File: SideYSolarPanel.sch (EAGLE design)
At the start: 35 parts

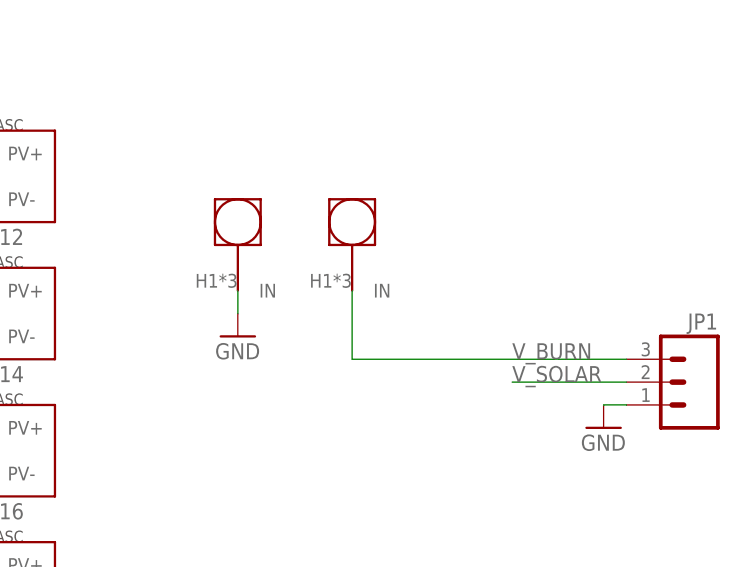
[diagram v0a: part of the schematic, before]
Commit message: Swapped X and Y solar panels per NanoRacks ICD
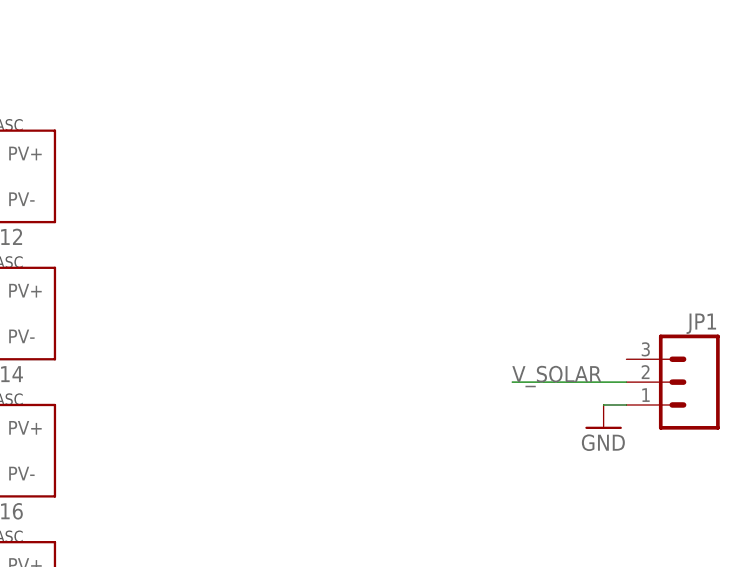
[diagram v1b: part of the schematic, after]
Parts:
- removed U$1, U$2: BURNER, Burner:BURNER
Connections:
- removed net V_BURN: JP1.3, U$1.IN
- net GND: no longer U$2.IN
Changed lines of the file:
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@@
 <part name="GND2" library="SparkFun" deviceset="GND" device=""/>
 <part name="JP1" library="SparkFun-Connectors" deviceset="M03" device="POLAR_LOCK"/>
-<part name="U$1" library="Burner" deviceset="BURNER" device=""/>
-<part name="U$2" library="Burner" deviceset="BURNER" device=""/>
-<part name="GND3" library="SparkFun" deviceset="GND" device=""/>
 </parts>
 <sheets>
@@
 <instance part="GND2" gate="1" x="172.72" y="60.96"/>
 <instance part="JP1" gate="G$1" x="182.88" y="66.04" rot="MR0"/>
-<instance part="U$1" gate="G$1" x="144.78" y="81.28"/>
-<instance part="U$2" gate="G$1" x="132.08" y="81.28"/>
-<instance part="GND3" gate="1" x="132.08" y="71.12"/>
 </instances>
 <busses>
@@
 <wire x1="172.72" y1="63.5" x2="175.26" y2="63.5" width="0.1524" layer="91"/>
 </segment>
-<segment>
-<pinref part="GND3" gate="1" pin="GND"/>
-<pinref part="U$2" gate="G$1" pin="IN"/>
-<wire x1="132.08" y1="73.66" x2="132.08" y2="76.2" width="0.1524" layer="91"/>
-</segment>
 </net>
 <net name="N$36" class="0">
@@
 </segment>
 </net>
-<net name="V_BURN" class="0">
-<segment>
-<pinref part="JP1" gate="G$1" pin="3"/>
-<label x="162.56" y="68.58" size="1.778" layer="95"/>
-<pinref part="U$1" gate="G$1" pin="IN"/>
-<wire x1="175.26" y1="68.58" x2="144.78" y2="68.58" width="0.1524" layer="91"/>
-<wire x1="144.78" y1="68.58" x2="144.78" y2="76.2" width="0.1524" layer="91"/>
-</segment>
-</net>

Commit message: Cleanup
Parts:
- added FRAME1: FRAME-LETTER, SparkFun-Aesthetics:FRAME-LETTER
- added U$1: KICKSAT_LOGO, KickSat-Logo:KICKSAT_LOGO
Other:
- note added: "Zac Manchester"
- moved on the sheet: D1, D10, D11, D12, D2, D3, D4, D5, D6, D7, D8, D9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

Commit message: Fixed solar cell footprints
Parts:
- D1, D10, D11, D12, D2, D3, D4, D5, D6, D7, D8, D9: device phonesat:SB_DIODE -> Solar:SB_DIODE
- S1, S10, S11, S12, S13, S14, S15, S16, S17, S18, S19, S2, S20, S3, S4, S5, S6, S7, S8, S9: device phonesat:SOLAR_CELL -> Solar:SOLAR_CELL
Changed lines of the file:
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@@
 </classes>
 <parts>
-<part name="S3" library="phonesat" deviceset="SOLAR_CELL" device=""/>
-<part name="D2" library="phonesat" deviceset="SB_DIODE" device=""/>
-<part name="S18" library="phonesat" deviceset="SOLAR_CELL" device=""/>
-<part name="S17" library="phonesat" deviceset="SOLAR_CELL" device=""/>
-<part name="S2" library="phonesat" deviceset="SOLAR_CELL" device=""/>
-<part name="S19" library="phonesat" deviceset="SOLAR_CELL" device=""/>
-<part name="S20" library="phonesat" deviceset="SOLAR_CELL" device=""/>
-<part name="S1" library="phonesat" deviceset="SOLAR_CELL" device=""/>
-<part name="S15" library="phonesat" deviceset="SOLAR_CELL" device=""/>
-<part name="S4" library="phonesat" deviceset="SOLAR_CELL" device=""/>
-<part name="S8" library="phonesat" deviceset="SOLAR_CELL" device=""/>
-<part name="S7" library="phonesat" deviceset="SOLAR_CELL" device=""/>
-<part name="S9" library="phonesat" deviceset="SOLAR_CELL" device=""/>
-<part name="S10" library="phonesat" deviceset="SOLAR_CELL" device=""/>
-<part name="S5" library="phonesat" deviceset="SOLAR_CELL" device=""/>
-<part name="S6" library="phonesat" deviceset="SOLAR_CELL" device=""/>
-<part name="D1" library="phonesat" deviceset="SB_DIODE" device=""/>
-<part name="D3" library="phonesat" deviceset="SB_DIODE" device=""/>
-<part name="D4" library="phonesat" deviceset="SB_DIODE" device=""/>
-<part name="D5" library="phonesat" deviceset="SB_DIODE" device=""/>
-<part name="D6" library="phonesat" deviceset="SB_DIODE" device=""/>
-<part name="D7" library="phonesat" deviceset="SB_DIODE" device=""/>
-<part name="D8" library="phonesat" deviceset="SB_DIODE" device=""/>
-<part name="D9" library="phonesat" deviceset="SB_DIODE" device=""/>
-<part name="D10" library="phonesat" deviceset="SB_DIODE" device=""/>
-<part name="D11" library="phonesat" deviceset="SB_DIODE" device=""/>
-<part name="D12" library="phonesat" deviceset="SB_DIODE" device=""/>
+<part name="S3" library="Solar" deviceset="SOLAR_CELL" device=""/>
+<part name="D2" library="Solar" deviceset="SB_DIODE" device=""/>
+<part name="S18" library="Solar" deviceset="SOLAR_CELL" device=""/>
+<part name="S17" library="Solar" deviceset="SOLAR_CELL" device=""/>
+<part name="S2" library="Solar" deviceset="SOLAR_CELL" device=""/>
+<part name="S19" library="Solar" deviceset="SOLAR_CELL" device=""/>
+<part name="S20" library="Solar" deviceset="SOLAR_CELL" device=""/>
+<part name="S1" library="Solar" deviceset="SOLAR_CELL" device=""/>
+<part name="S15" library="Solar" deviceset="SOLAR_CELL" device=""/>
+<part name="S4" library="Solar" deviceset="SOLAR_CELL" device=""/>
+<part name="S8" library="Solar" deviceset="SOLAR_CELL" device=""/>
+<part name="S7" library="Solar" deviceset="SOLAR_CELL" device=""/>
+<part name="S9" library="Solar" deviceset="SOLAR_CELL" device=""/>
+<part name="S10" library="Solar" deviceset="SOLAR_CELL" device=""/>
+<part name="S5" library="Solar" deviceset="SOLAR_CELL" device=""/>
+<part name="S6" library="Solar" deviceset="SOLAR_CELL" device=""/>
+<part name="D1" library="Solar" deviceset="SB_DIODE" device=""/>
+<part name="D3" library="Solar" deviceset="SB_DIODE" device=""/>
+<part name="D4" library="Solar" deviceset="SB_DIODE" device=""/>
+<part name="D5" library="Solar" deviceset="SB_DIODE" device=""/>
+<part name="D6" library="Solar" deviceset="SB_DIODE" device=""/>
+<part name="D7" library="Solar" deviceset="SB_DIODE" device=""/>
+<part name="D8" library="Solar" deviceset="SB_DIODE" device=""/>
+<part name="D9" library="Solar" deviceset="SB_DIODE" device=""/>
+<part name="D10" library="Solar" deviceset="SB_DIODE" device=""/>
+<part name="D11" library="Solar" deviceset="SB_DIODE" device=""/>
+<part name="D12" library="Solar" deviceset="SB_DIODE" device=""/>
 <part name="GND1" library="SparkFun" deviceset="GND" device=""/>
-<part name="S11" library="phonesat" deviceset="SOLAR_CELL" device=""/>
-<part name="S16" library="phonesat" deviceset="SOLAR_CELL" device=""/>
-<part name="S12" library="phonesat" deviceset="SOLAR_CELL" device=""/>
-<part name="S14" library="phonesat" deviceset="SOLAR_CELL" device=""/>
-<part name="S13" library="phonesat" deviceset="SOLAR_CELL" device=""/>
+<part name="S11" library="Solar" deviceset="SOLAR_CELL" device=""/>
+<part name="S16" library="Solar" deviceset="SOLAR_CELL" device=""/>
+<part name="S12" library="Solar" deviceset="SOLAR_CELL" device=""/>
+<part name="S14" library="Solar" deviceset="SOLAR_CELL" device=""/>
+<part name="S13" library="Solar" deviceset="SOLAR_CELL" device=""/>
 <part name="GND2" library="SparkFun" deviceset="GND" device=""/>
 <part name="JP1" library="SparkFun-Connectors" deviceset="M03" device="POLAR_LOCK"/>
